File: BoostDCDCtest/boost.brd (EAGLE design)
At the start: 160 x 100 mm, 28 parts, among them IC1 SI8235-IS1, M1 FET_ON_SOCKET

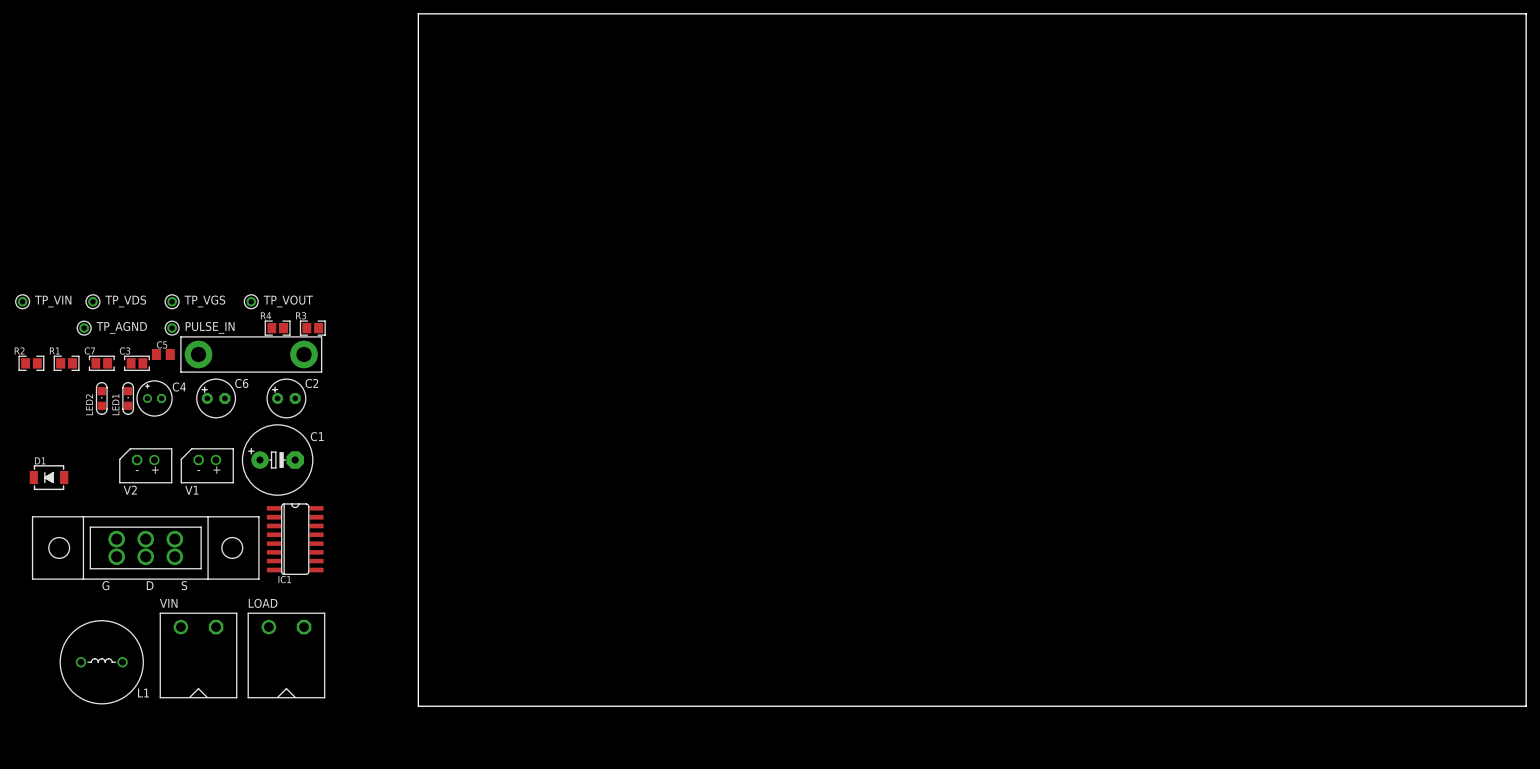
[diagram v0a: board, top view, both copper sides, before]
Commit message: 1st brd completed
sch has been also editted because there is some issues of tolerance in the test situation.
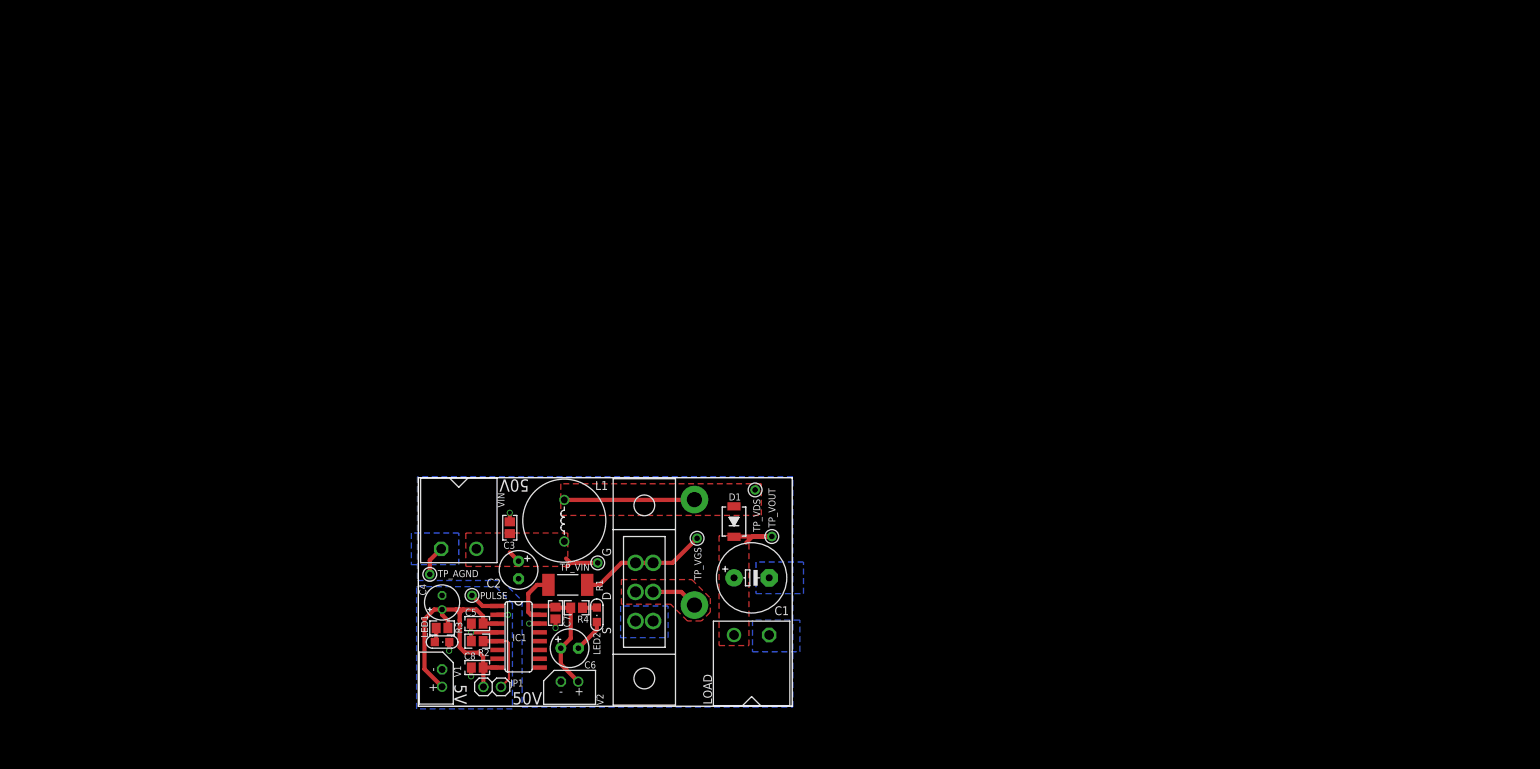
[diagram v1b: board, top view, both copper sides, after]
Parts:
- removed PULSE_IN: PIN, lab:PIN
- added C8: 0.1u, resistor:C0805
- added JP1: (no value), pinhead:1X02
- added PULSE: PIN, lab:PIN
- C5: device rcl:C0805K -> resistor:C0805
- R1: device resistor:R0805 -> resistor:R2512
- moved TP_VDS 99.4 mm to (48.6, 31.2)
- moved D1 99.1 mm to (45.6, 26.7), turned to 90 degrees
- moved TP_VIN 91.2 mm to (25.9, 20.7), turned to 180 degrees
- moved TP_VGS 83.2 mm to (40.3, 24.3), turned to 90 degrees
- moved TP_VOUT 82.5 mm to (51.1, 24.5), turned to 90 degrees
- moved R1 79.1 mm to (21.6, 17.5), turned to 180 degrees
- moved LED2 78.0 mm to (25.8, 13.2), turned to 180 degrees
- moved R2 75.9 mm to (8.51, 9.40)
- moved C7 74.8 mm to (19.8, 13.5), turned to 270 degrees
- moved M1 72.3 mm to (32.6, 16.5), turned to 270 degrees
- moved C1 70.5 mm to (48.1, 18.5)
- moved U$1 70.1 mm to (39.9, 22.2), flipped to the bottom, turned to 90 degrees
- moved L1 69.9 mm to (21.1, 26.8), turned to 90 degrees
- moved V2 69.1 mm to (21.8, 3.56)
- moved LOAD 67.2 mm to (48.1, 10.3)
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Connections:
- net +5V: now also C8.1, JP1.2
- net GND: now also C8.2
- net N$5: now also JP1.1
- net N$6: now also PULSE.1; no longer PULSE_IN.1
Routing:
- net +5V: track 0.00 -> 44.1 mm
- net N$2: track 0.00 -> 18.8 mm
- net N$3: track 0.00 -> 18.7 mm
- net V+: track 0.00 -> 16.9 mm
- net AGND: track 0.00 -> 13.4 mm, vias 0 -> 3
- net N$5: track 0.00 -> 10.7 mm
- net GND: track 0.00 -> 10.5 mm, vias 0 -> 4
- net N$7: track 0.00 -> 9.53 mm
- net GATE: track 0.00 -> 7.94 mm
- net N$1: track 0.00 -> 7.35 mm
- net N$4: track 0.00 -> 6.76 mm
- net N$6: track 0.00 -> 4.29 mm
- net N$8: track 0.00 -> 2.11 mm
- net N$9: track 0.00 -> 2.09 mm
- added copper zone on layer 16, net AGND
- added copper zone on layer 16, net GND
- added copper zone on layer 1, net N$1
- added copper zone on layer 1, net N$2
- added copper zone on layer 1, net N$4
- added copper zone on layer 1, net N$7
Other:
- board size 160 x 100 mm -> 54 x 33 mm
- board text added: "50V"
- board text added: "5V"

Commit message: add 4 fixing-arms
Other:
- board size 54 x 33 mm -> 68 x 47 mm
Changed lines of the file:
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@@
 <setting verticaltext="up"/>
 </settings>
-<grid distance="5" unitdist="mil" unit="mil" style="lines" multiple="1" display="yes" altdistance="5" altunitdist="mil" altunit="mil"/>
+<grid distance="1" unitdist="mm" unit="mm" style="lines" multiple="1" display="yes" altdistance="5" altunitdist="mil" altunit="mil"/>
 <layers>
 <layer number="1" name="Top" color="4" fill="1" visible="yes" active="yes"/>
@@
 <board>
 <plain>
-<wire x1="0" y1="0" x2="54" y2="0" width="0" layer="20"/>
-<wire x1="54" y1="0" x2="54" y2="33" width="0" layer="20"/>
-<wire x1="54" y1="33" x2="0" y2="33" width="0" layer="20"/>
-<wire x1="0" y1="33" x2="0" y2="0" width="0" layer="20"/>
+<wire x1="53" y1="-3" x2="50" y2="0" width="0" layer="20"/>
+<wire x1="50" y1="0" x2="4" y2="0" width="0" layer="20"/>
+<wire x1="4" y1="0" x2="1" y2="-3" width="0" layer="20"/>
 <text x="5.207" y="3.175" size="1.778" layer="21" rot="SR270">5V</text>
 <text x="13.589" y="0.254" size="1.778" layer="21" rot="SR0">50V</text>
+<wire x1="57" y1="32" x2="54" y2="29" width="0" layer="20"/>
+<wire x1="54" y1="29" x2="54" y2="4" width="0" layer="20"/>
+<wire x1="54" y1="4" x2="57" y2="1" width="0" layer="20"/>
+<wire x1="1" y1="36" x2="4" y2="33" width="0" layer="20"/>
+<wire x1="4" y1="33" x2="50" y2="33" width="0" layer="20"/>
+<wire x1="50" y1="33" x2="53" y2="36" width="0" layer="20"/>
+<wire x1="-3" y1="32" x2="0" y2="29" width="0" layer="20"/>
+<wire x1="-3" y1="1" x2="0" y2="4" width="0" layer="20"/>
+<wire x1="0" y1="4" x2="0" y2="29" width="0" layer="20"/>
 <wire x1="7.62" y1="25.781" x2="5.969" y2="24.13" width="0.6096" layer="41"/>
 <wire x1="5.715" y1="21.336" x2="7.62" y2="19.431" width="0.6096" layer="41"/>
@@
 <wire x1="54.229" y1="9.906" x2="44.196" y2="-0.127" width="0.254" layer="42"/>
 <wire x1="19.939" y1="-0.254" x2="14.732" y2="4.953" width="0.254" layer="42"/>
-<dimension x1="0" y1="33" x2="0" y2="0" x3="-3" y3="16.5" textsize="1.778" layer="48"/>
-<dimension x1="0" y1="33" x2="54" y2="33" x3="27" y3="36" textsize="1.778" layer="48"/>
 <wire x1="2.286" y1="17.526" x2="0.254" y2="15.494" width="0.254" layer="42"/>
 <wire x1="0.254" y1="2.54" x2="2.54" y2="0.254" width="0.254" layer="42"/>
@@
 <wire x1="13.335" y1="29.464" x2="15.113" y2="27.686" width="0.6096" layer="42"/>
 <wire x1="19.685" y1="28.448" x2="21.336" y2="26.797" width="0.6096" layer="41"/>
+<wire x1="-3" y1="1" x2="-7" y2="-3" width="0" layer="20" curve="90"/>
+<wire x1="-7" y1="-3" x2="-3" y2="-7" width="0" layer="20" curve="90"/>
+<wire x1="-3" y1="-7" x2="1" y2="-3" width="0" layer="20" curve="90"/>
+<wire x1="-3" y1="40" x2="-7" y2="36" width="0" layer="20" curve="90"/>
+<wire x1="-3" y1="32" x2="-7" y2="36" width="0" layer="20" curve="-90"/>
+<wire x1="-3" y1="40" x2="1" y2="36" width="0" layer="20" curve="-90"/>
+<wire x1="57" y1="40" x2="53" y2="36" width="0" layer="20" curve="90"/>
+<wire x1="57" y1="40" x2="61" y2="36" width="0" layer="20" curve="-90"/>
+<wire x1="57" y1="32" x2="61" y2="36" width="0" layer="20" curve="90"/>
+<wire x1="57" y1="1" x2="61" y2="-3" width="0" layer="20" curve="-90"/>
+<wire x1="57" y1="-7" x2="61" y2="-3" width="0" layer="20" curve="90"/>
+<wire x1="57" y1="-7" x2="53" y2="-3" width="0" layer="20" curve="-90"/>
+<dimension x1="54" y1="29" x2="0" y2="29" x3="27" y3="41" textsize="1.778" layer="48"/>
+<dimension x1="4" y1="33" x2="4" y2="0" x3="-8" y3="16.5" textsize="1.778" layer="48"/>
+<dimension x1="-7" y1="36" x2="61" y2="36" x3="27" y3="45" textsize="1.778" layer="48"/>
+<dimension x1="-3" y1="40" x2="-3" y2="-7" x3="-12" y3="16.5" textsize="1.778" layer="48"/>
 </plain>
 <attributes>
@@
 <wire x1="5.969" y1="13.462" x2="6.477" y2="13.97" width="0.6096" layer="1"/>
 </signal>
+<signal name="N$10">
+<via x="-3" y="36" extent="1-16" drill="3.1" diameter="6"/>
+</signal>
+<signal name="N$11">
+<via x="-3" y="-3" extent="1-16" drill="3.1" diameter="6"/>
+</signal>
+<signal name="N$12">
+<via x="57" y="36" extent="1-16" drill="3.1" diameter="6"/>
+</signal>
+<signal name="N$13">
+<via x="57" y="-3" extent="1-16" drill="3.1" diameter="6"/>
+</signal>
 </signals>
